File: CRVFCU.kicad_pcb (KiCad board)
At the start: 4 copper layers, 50 x 100 mm, 157 parts, among them J1 TagConnect_TC2030, J2 Conn_01x02, J3 USB_C_Receptacle_USB2.0_16P, J4 Micro_SD_Card_Det2, J5 Conn_01x02, Q3 DMG2301L, Q4 BC818, Q5 DMG2301L, Q6 DMG2301L, U1 MS5611-01BA, U10 W25Q128JVS, U11 EClamp2515K, U12 ESDALC6V1W5, U13 USBLC6-2SC6, U14 USBLC6-2SC6, U15 MAX17049, U16 SI7232DN-T1, U17 SN74LV1T34DCK, U2 STM32H747IITx, U3 LIS2MDL, U4 ICM-45686, U5 FXMA108, U6 AP1117-50, U7 AP1117-33, U8 SI7232DN-T1, U9 USBLC6-4SC6, Y1 32.768khz, Y2 Crystal_GND24, Y3 32.768khz

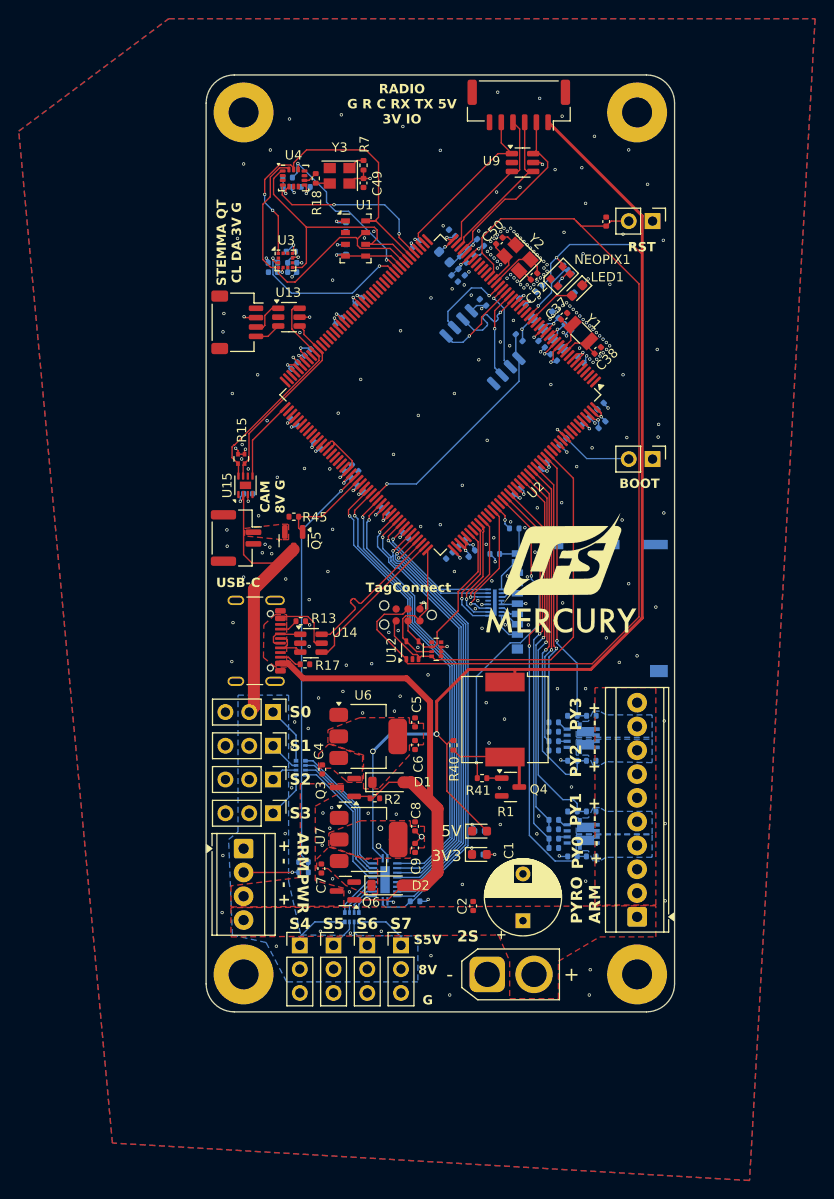
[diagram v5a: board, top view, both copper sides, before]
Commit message: changed via sizes for manufacturing purposes and fixed drc
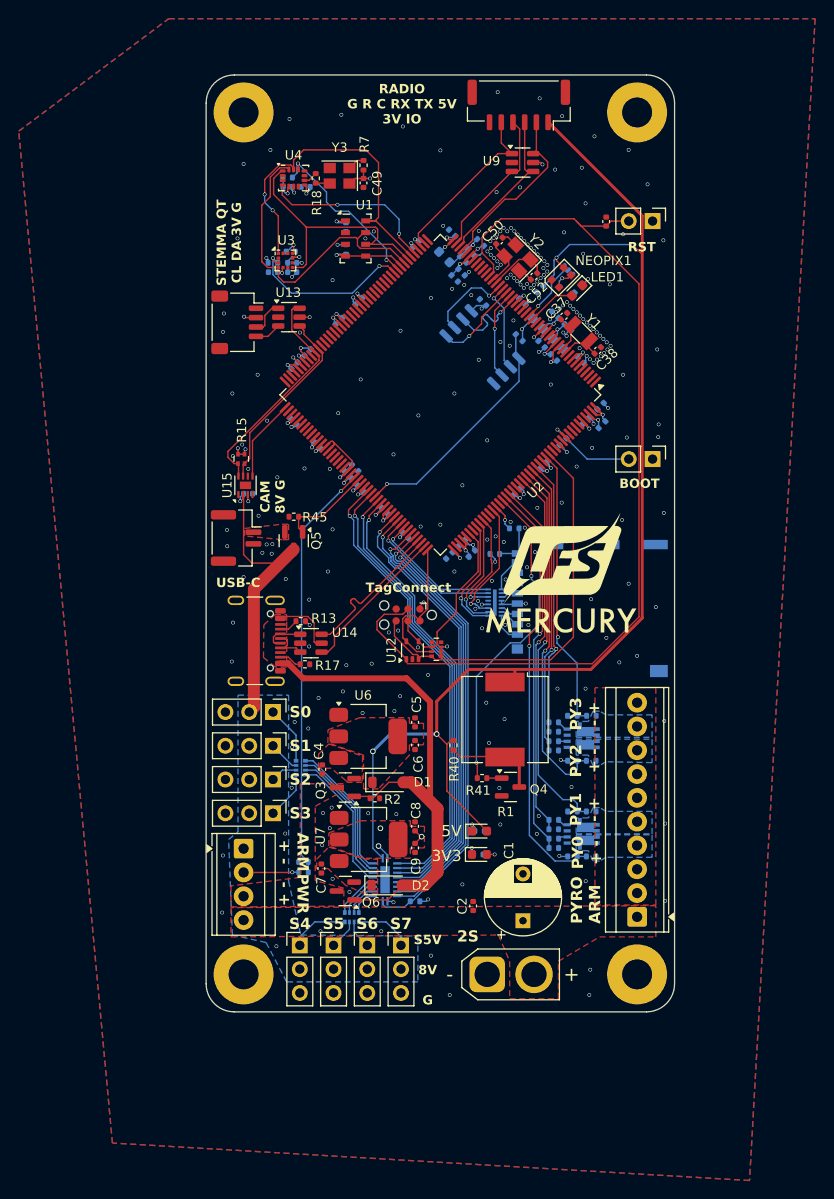
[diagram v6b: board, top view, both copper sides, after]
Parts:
- C37, C38: value 6pF -> 4pF
- C50, C52: value 10pF -> 12pF
- Y1: value 32.768khz -> ECS-.327-6-34QCS-TR
- Y2: value Crystal_GND24 -> ECS-250-10-33B-CKY-TR3
- moved NEOPIX1 0.16 mm to (77.9, 41.6)
- moved U17 0.08 mm to (78.0, 41.5)
- moved C53 0.07 mm to (75.6, 42.9)
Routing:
- net +3V3: track 88.1 -> 89.2 mm
- net /SDA: track 24.6 -> 25.2 mm
- net /MOSI: track 32.7 -> 33.2 mm
- net /SRVI_1: track 46.5 -> 47.0 mm
